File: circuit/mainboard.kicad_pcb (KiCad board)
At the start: 2 copper layers, 59 x 100 mm, 29 parts, among them J1 MOTOR_CONN, J10 BEAM_EMIT_RIGHT, J11 UNUSED_PINS, J2 CTRLR_CONN, J3 DISP_LEFT, J4 DISP_RIGHT, J6 LED_Conn, J7 BEAM_SENSE_LEFT, J8 BEAM_SENSE_RIGHT, J9 BEAM_EMIT_LEFT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

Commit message: route PCB
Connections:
- net Net-(BT1-+) renamed /PRESWITCH
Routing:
- net 5V: track 0.00 -> 168.6 mm
- net +3V3: track 0.00 -> 153.5 mm, vias 0 -> 4
- net /CTRL_LEDRACE: track 0.00 -> 103.9 mm, vias 0 -> 2
- net /CTRL_LEDARM: track 0.00 -> 99.6 mm, vias 0 -> 2
- net /SCL: track 0.00 -> 96.9 mm, vias 0 -> 2
- net /SDA: track 0.00 -> 94.0 mm, vias 0 -> 3
- net /MTR_RX: track 0.00 -> 87.5 mm, vias 0 -> 4
- net /MTR_PRES: track 0.00 -> 83.2 mm, vias 0 -> 2
- net /MTR_TX: track 0.00 -> 79.9 mm, vias 0 -> 4
- net /MTR_DISCRIM: track 0.00 -> 76.4 mm, vias 0 -> 2
- net /RBEAM_SIG: track 0.00 -> 70.6 mm, vias 0 -> 2
- net /LBEAM_SIG: track 0.00 -> 61.0 mm, vias 0 -> 2
- net /CTRL_DISCRIM: track 0.00 -> 58.4 mm, vias 0 -> 2
- net /CTRL_PRES: track 0.00 -> 52.4 mm
- net /CTRL_ARM: track 0.00 -> 47.6 mm
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- added copper zone on B.Cu, net GND
- added copper zone on F.Cu, net GND
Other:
- rule pad_to_mask_clearance: 0 -> 0.038

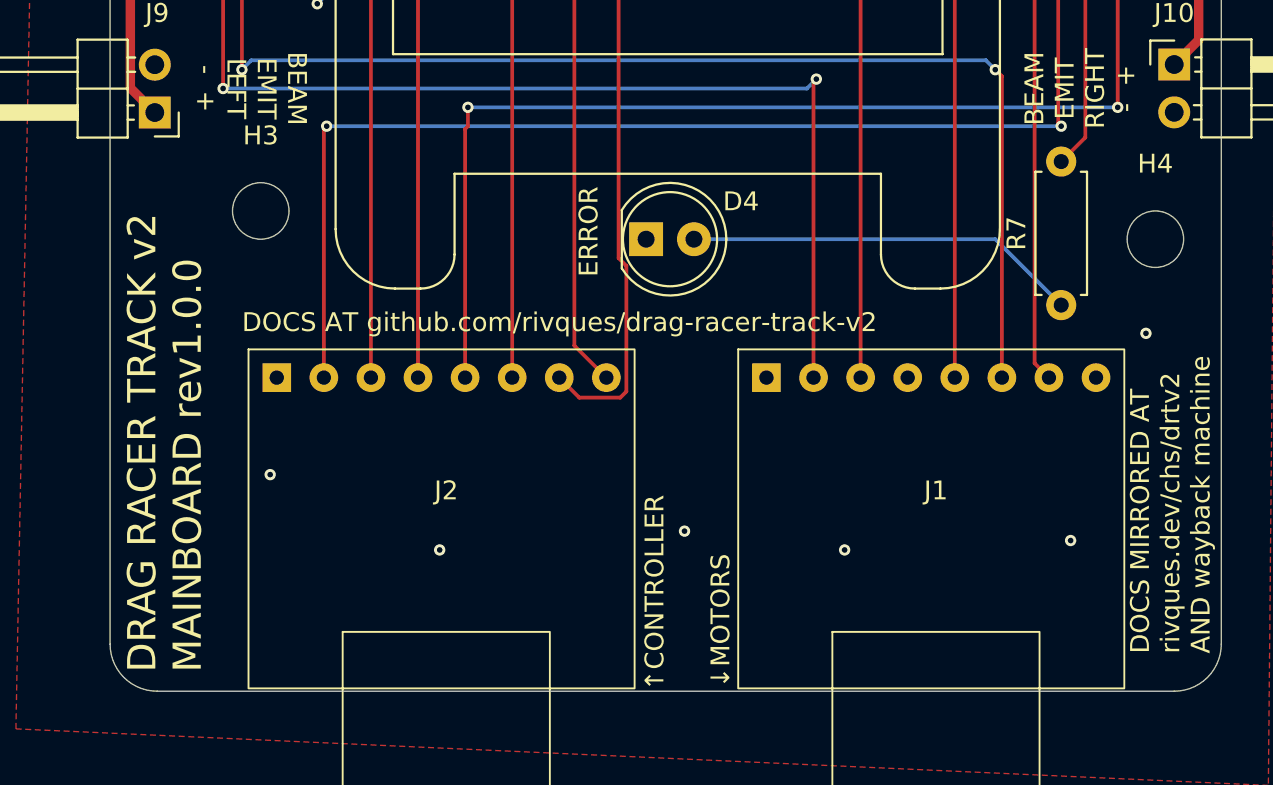
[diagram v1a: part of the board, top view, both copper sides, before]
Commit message: refine PCB
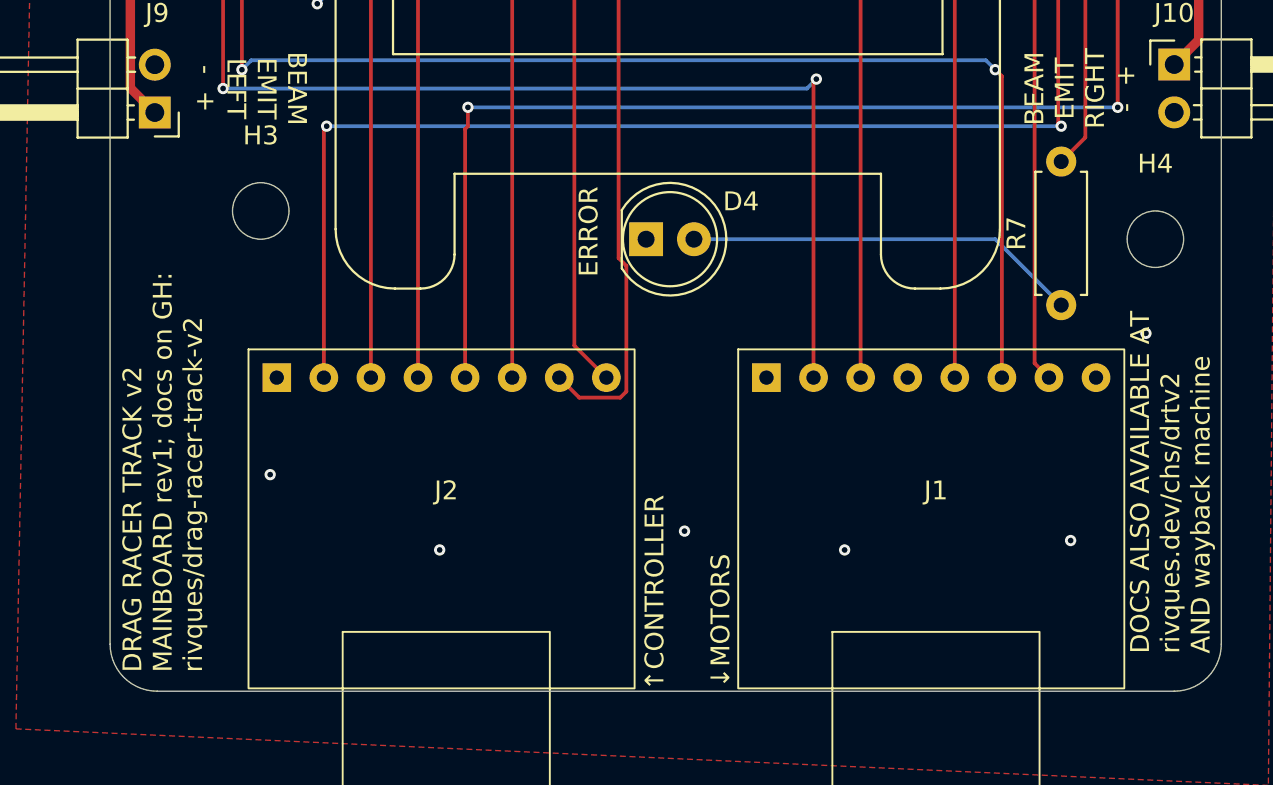
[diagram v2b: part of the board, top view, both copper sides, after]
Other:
- board text added: "DOCS ALSO AVAILABLE AT rivques.dev/chs/drtv2 AND wayback machine"
- board text added: "DRAG RACER TRACK v2 MAINBOARD rev1; docs on GH: rivques/drag-racer-track-v2"
- board text removed: "DOCS AT github.com/rivques/drag-racer-track-v2"
- board text removed: "DOCS MIRRORED AT rivques.dev/chs/drtv2 AND wayback machine"
- board text removed: "DRAG RACER TRACK v2 MAINBOARD rev1.0.0"
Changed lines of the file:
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@@
 			(plot_on_all_layers_selection 0x0000000_00000000)
 			(disableapertmacros no)
-			(usegerberextensions no)
-			(usegerberattributes yes)
+			(usegerberextensions yes)
+			(usegerberattributes no)
 			(usegerberadvancedattributes yes)
-			(creategerberjobfile yes)
+			(creategerberjobfile no)
 			(dashed_line_dash_ratio 12.000000)
 			(dashed_line_gap_ratio 3.000000)
@@
 			(psa4output no)
 			(plotreference yes)
-			(plotvalue yes)
+			(plotvalue no)
 			(plotfptext yes)
 			(plotinvisibletext no)
 			(sketchpadsonfab no)
-			(subtractmaskfromsilk no)
+			(subtractmaskfromsilk yes)
 			(outputformat 1)
 			(mirror no)
-			(drillshape 1)
+			(drillshape 0)
 			(scaleselection 1)
-			(outputdirectory "")
+			(outputdirectory "production/")
 		)
 	)
@@
 		(layer "Edge.Cuts")
 	)
-	(gr_text "DOCS AT github.com/rivques/drag-racer-track-v2"
-		(at 141 128 0)
-		(layer "F.SilkS")
-		(effects
-			(font
-				(size 1 1)
-				(thickness 0.1)
-			)
-			(justify left bottom)
-		)
-	)
 	(gr_text "DISPLAY\nRIGHT\n- SCL SDA +"
 		(at 188.5 94 90)
@@
 		)
 	)
-	(gr_text "DOCS MIRRORED AT\nrivques.dev/chs/drtv2\nAND wayback machine"
+	(gr_text "DOCS ALSO AVAILABLE AT\nrivques.dev/chs/drtv2\nAND wayback machine"
 		(at 192.5 145 90)
 		(layer "F.SilkS")
@@
 		)
 	)
-	(gr_text "DRAG RACER TRACK v2\nMAINBOARD rev1.0.0"
+	(gr_text "DRAG RACER TRACK v2\nMAINBOARD rev1; docs on GH:\nrivques/drag-racer-track-v2"
 		(at 139 146 90)
 		(layer "F.SilkS")
 		(effects
 			(font
-				(size 1.5 1.5)
+				(size 1 1)
 				(thickness 0.1)
 			)

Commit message: This is the board that was produced as rev1
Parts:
- added D5: 1N4001, Diode_THT:D_DO-41_SOD81_P10.16mm_Horizontal, F.Cu at (152.6, 54.5)
- added JP1: ~, Jumper:SolderJumper-2_P1.3mm_Open_TrianglePad1.0x1.5mm, F.Cu at (160.0, 96.3)
- added JP2: ~, Jumper:SolderJumper-2_P1.3mm_Open_TrianglePad1.0x1.5mm, F.Cu at (162.5, 96.3)
- added JP3: ~, Jumper:SolderJumper-2_P1.3mm_Open_TrianglePad1.0x1.5mm, F.Cu at (165.0, 96.2)
- added JP4: ~, Jumper:SolderJumper-2_P1.3mm_Open_TrianglePad1.0x1.5mm, F.Cu at (167.5, 96.2)
- C2: footprint Capacitor_THT:CP_Radial_D4.0mm_P2.00mm -> Capacitor_THT:CP_Radial_D5.0mm_P2.00mm
- moved C2 13.9 mm to (153.0, 61.0)
- moved SW1 11.6 mm to (144.9, 49.5), turned to 90 degrees
- moved U2 7.46 mm to (142.0, 60.0), turned to 0 degrees
- moved C1 2.92 mm to (157.5, 59.5)
- moved BT1 0.62 mm to (136.5, 59.3)
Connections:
- A2 pad 39: 5V -> /VSYS
- U1 pad 3: unconnected-(U1-A0-Pad3) -> Net-(JP1-A)
- U1 pad 4: unconnected-(U1-RST-Pad4) -> Net-(JP2-A)
- U1 pad 5: unconnected-(U1-CS-Pad5) -> Net-(JP3-A)
- U1 pad 6: unconnected-(U1-3VO-Pad6) -> Net-(JP4-A)
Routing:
- net /SDA: track 94.0 -> 116.1 mm, vias 3 -> 5
- net /VSYS: track 0.00 -> 19.1 mm
- net /CTRL_PRES: track 52.4 -> 71.2 mm, vias 0 -> 4
- net 5V: track 168.6 -> 187.1 mm
- net /PRESWITCH: track 6.14 -> 23.6 mm
- net /SCL: track 96.9 -> 112.7 mm, vias 2 -> 4
- net +3V3: track 153.5 -> 167.9 mm, vias 4 -> 6
- net /VBAT: track 10.7 -> 23.4 mm
- net Net-(JP1-A): track 0.00 -> 2.63 mm
- net Net-(JP2-A): track 0.00 -> 2.62 mm
- net Net-(JP3-A): track 0.00 -> 2.55 mm
- net Net-(JP4-A): track 0.00 -> 2.53 mm
- net GND: vias 29 -> 26
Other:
- board text added: "+ 1R 1G 2R 2G 3R 3G"
- board text added: "-BAT+"
- board text added: "ADAFRUIT OLED"
- board text added: "CLOSE JUMPERS FOR GENERIC OLED"
- board text added: "DRAG RACER TRACK v2 MAINBOARD rev1; docs on GH: rivques/drag-racer-track-v2 made by River Lewis in 2025"
- board text added: "JLCJLCJLCJLC"
- board text added: "RJ45 pinout: 1:GND|2:LED_RACE 3:Discrim|4:RESET 5:LED_ARM|6:ARM 7:Presence|8:RACE"
- board text added: "RJ45 pinout: 1:GND|2:TX 3:Discrim|4:NC 5:3V3|6:RX 7:Presence|8:NC"
- board text added: "RasPi Pico"
- board text added: "SparkFun RJ45 Breakout"
- board text added: "Unused pins: - 28 20 19 18 3V 5V"
- board text removed: "+"
- board text removed: "-"
- board text removed: "DRAG RACER TRACK v2 MAINBOARD rev1; docs on GH: rivques/drag-racer-track-v2"
